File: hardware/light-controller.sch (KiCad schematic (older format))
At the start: 15 parts

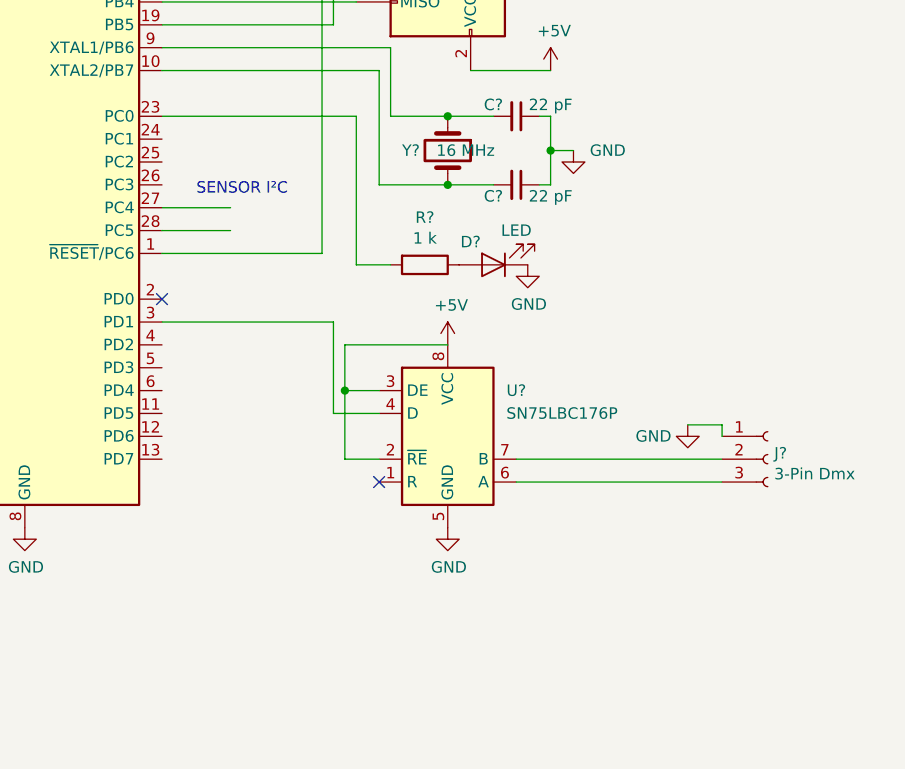
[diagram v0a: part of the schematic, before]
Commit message: Add distance sensor, make the light flicker when distance is small.
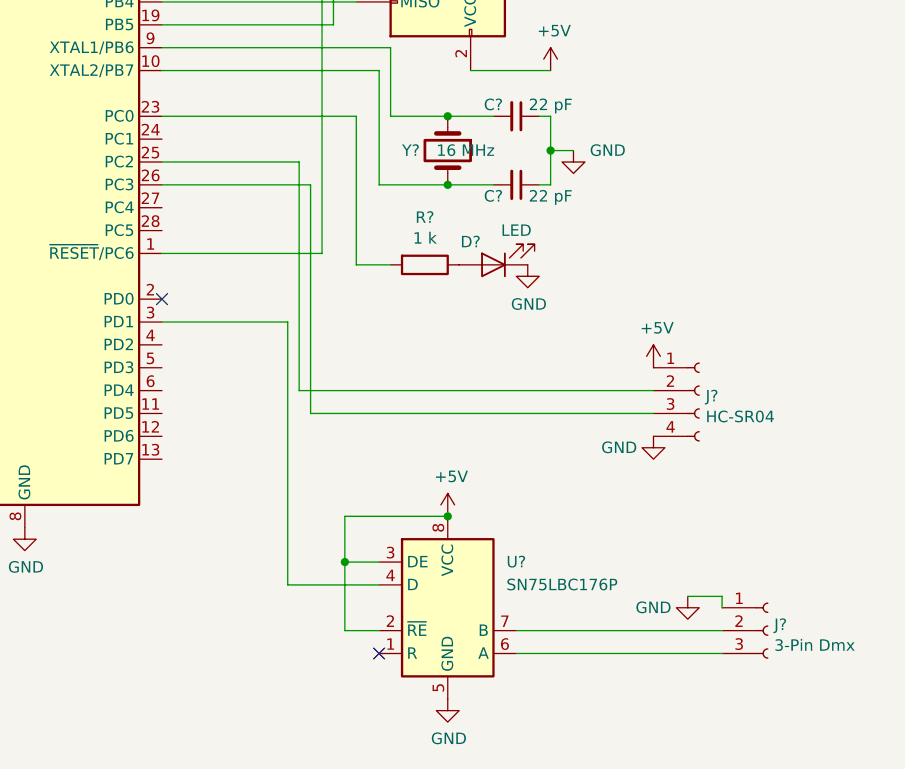
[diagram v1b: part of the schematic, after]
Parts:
- added J?: HC-SR04, symbol Connector:Conn_01x04_Female
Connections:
- wire segments 50 -> 54
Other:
- note removed: "SENSOR I²C"
- moved on the sheet: J?, U?
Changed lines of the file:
@@
 	4300 2850 5250 2850
 Connection ~ 5550 3350
-Wire Wire Line
-	4300 3450 4600 3450
-Wire Wire Line
-	4300 3550 4600 3550
-Text Notes 4450 3400 0    50   ~ 0
-SENSOR I²C
 $Comp
 L Device:LED D?
@@
 L Interface_UART:SN75LBC176P U?
 U 1 1 5DBC31FC
-P 5550 4450
-F 0 "U?" H 5850 4650 50  0000 C CNN
-F 1 "SN75LBC176P" H 6050 4550 50  0000 C CNN
-F 2 "Package_DIP:DIP-8_W7.62mm" H 5550 3950 50  0001 C CNN
-F 3 "http://www.ti.com/lit/ds/symlink/sn75lbc176.pdf" H 7150 4250 50  0001 C CNN
-	1    5550 4450
+P 5550 5200
+F 0 "U?" H 5850 5400 50  0000 C CNN
+F 1 "SN75LBC176P" H 6050 5300 50  0000 C CNN
+F 2 "Package_DIP:DIP-8_W7.62mm" H 5550 4700 50  0001 C CNN
+F 3 "http://www.ti.com/lit/ds/symlink/sn75lbc176.pdf" H 7150 5000 50  0001 C CNN
+	1    5550 5200
 	1    0    0    -1
 $EndComp
@@
 L power:+5V #PWR?
 U 1 1 5DBC51AD
-P 5550 4050
-F 0 "#PWR?" H 5550 3900 50  0001 C CNN
-F 1 "+5V" H 5565 4223 50  0000 C CNN
-F 2 "" H 5550 4050 50  0001 C CNN
-F 3 "" H 5550 4050 50  0001 C CNN
-	1    5550 4050
+P 5550 4800
+F 0 "#PWR?" H 5550 4650 50  0001 C CNN
+F 1 "+5V" H 5565 4973 50  0000 C CNN
+F 2 "" H 5550 4800 50  0001 C CNN
+F 3 "" H 5550 4800 50  0001 C CNN
+	1    5550 4800
 	1    0    0    -1
 $EndComp
@@
 L power:GND #PWR?
 U 1 1 5DBC5539
-P 5550 4850
-F 0 "#PWR?" H 5550 4600 50  0001 C CNN
-F 1 "GND" H 5555 4677 50  0000 C CNN
-F 2 "" H 5550 4850 50  0001 C CNN
-F 3 "" H 5550 4850 50  0001 C CNN
-	1    5550 4850
+P 5550 5600
+F 0 "#PWR?" H 5550 5350 50  0001 C CNN
+F 1 "GND" H 5555 5427 50  0000 C CNN
+F 2 "" H 5550 5600 50  0001 C CNN
+F 3 "" H 5550 5600 50  0001 C CNN
+	1    5550 5600
 	1    0    0    -1
 $EndComp
 Wire Wire Line
-	5550 4050 5100 4050
+	5550 4800 5100 4800
 Wire Wire Line
-	5100 4050 5100 4250
+	5100 4800 5100 5000
 Wire Wire Line
-	5100 4550 5250 4550
+	5100 5300 5250 5300
 Wire Wire Line
-	5250 4250 5100 4250
-Connection ~ 5100 4250
+	5250 5000 5100 5000
+Connection ~ 5100 5000
 Wire Wire Line
-	5100 4250 5100 4550
-Wire Wire Line
-	5250 4350 5050 4350
-Wire Wire Line
-	5050 4350 5050 3950
-Wire Wire Line
-	4300 3950 5050 3950
+	5100 5000 5100 5300
 $Comp
 L Connector:Conn_01x03_Female J?
 U 1 1 5DBD26D8
-P 6950 4550
-F 0 "J?" H 6978 4576 50  0000 L CNN
-F 1 "3-Pin Dmx" H 6978 4485 50  0000 L CNN
-F 2 "" H 6950 4550 50  0001 C CNN
-F 3 "~" H 6950 4550 50  0001 C CNN
-	1    6950 4550
+P 6950 5300
+F 0 "J?" H 6978 5326 50  0000 L CNN
+F 1 "3-Pin Dmx" H 6978 5235 50  0000 L CNN
+F 2 "" H 6950 5300 50  0001 C CNN
+F 3 "~" H 6950 5300 50  0001 C CNN
+	1    6950 5300
 	1    0    0    -1
 $EndComp
 Wire Wire Line
-	5850 4650 6750 4650
+	5850 5400 6750 5400
 Wire Wire Line
-	5850 4550 6750 4550
+	5850 5300 6750 5300
 $Comp
 L power:GND #PWR?
 U 1 1 5DBD48AF
-P 6600 4400
-F 0 "#PWR?" H 6600 4150 50  0001 C CNN
-F 1 "GND" H 6450 4350 50  0000 C CNN
-F 2 "" H 6600 4400 50  0001 C CNN
-F 3 "" H 6600 4400 50  0001 C CNN
-	1    6600 4400
+P 6600 5150
+F 0 "#PWR?" H 6600 4900 50  0001 C CNN
+F 1 "GND" H 6450 5100 50  0000 C CNN
+F 2 "" H 6600 5150 50  0001 C CNN
+F 3 "" H 6600 5150 50  0001 C CNN
+	1    6600 5150
 	1    0    0    -1
 $EndComp
 Wire Wire Line
-	6750 4450 6750 4400
+	6750 5200 6750 5150
 Wire Wire Line
-	6750 4400 6600 4400
+	6750 5150 6600 5150
 NoConn ~ 4300 3850
-NoConn ~ 5250 4650
+NoConn ~ 5250 5400
+Connection ~ 5550 4800
+Wire Wire Line
+	4850 5100 4850 3950
+Wire Wire Line
+	4850 3950 4300 3950
+Wire Wire Line
+	4850 5100 5250 5100
+$Comp
+L Connector:Conn_01x04_Female J?
+U 1 1 5DBDC32E
+P 6650 4250
+F 0 "J?" H 6678 4226 50  0000 L CNN
+F 1 "HC-SR04" H 6678 4135 50  0000 L CNN
+F 2 "" H 6650 4250 50  0001 C CNN
+F 3 "~" H 6650 4250 50  0001 C CNN
+	1    6650 4250
+	1    0    0    -1
+$EndComp
+$Comp
+L power:GND #PWR?
+U 1 1 5DBDD1C5
+P 6450 4450
+F 0 "#PWR?" H 6450 4200 50  0001 C CNN
+F 1 "GND" H 6300 4400 50  0000 C CNN
+F 2 "" H 6450 4450 50  0001 C CNN
+F 3 "" H 6450 4450 50  0001 C CNN
+	1    6450 4450
+	1    0    0    -1
+$EndComp
+$Comp
+L power:+5V #PWR?
+U 1 1 5DBE2390
+P 6450 4150
+F 0 "#PWR?" H 6450 4000 50  0001 C CNN
+F 1 "+5V" H 6465 4323 50  0000 C CNN
+F 2 "" H 6450 4150 50  0001 C CNN
+F 3 "" H 6450 4150 50  0001 C CNN
+	1    6450 4150
+	1    0    0    -1
+$EndComp
+Wire Wire Line
+	4300 3350 4950 3350
+Wire Wire Line
+	4950 4350 6450 4350
+Wire Wire Line
+	4950 3350 4950 4350
+Wire Wire Line
+	6450 4250 4900 4250
+Wire Wire Line
+	4900 3250 4300 3250
+Wire Wire Line
+	4900 3250 4900 4250
 $EndSCHEMATC
